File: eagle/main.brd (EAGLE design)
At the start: 100 x 95 mm, 31 parts, among them IC1 STM32F103, IC2 LM1117, Q1 8MHz

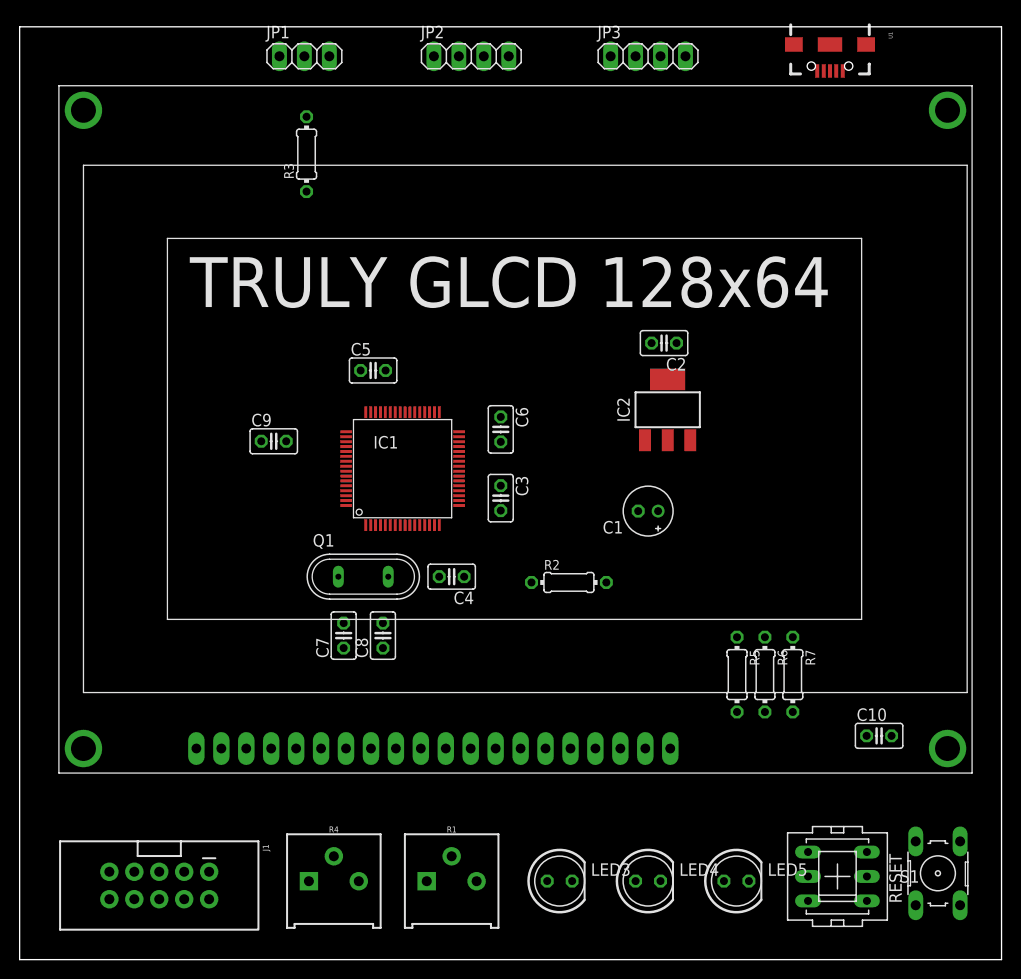
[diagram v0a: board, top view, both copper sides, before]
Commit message: Route some nets in the main board
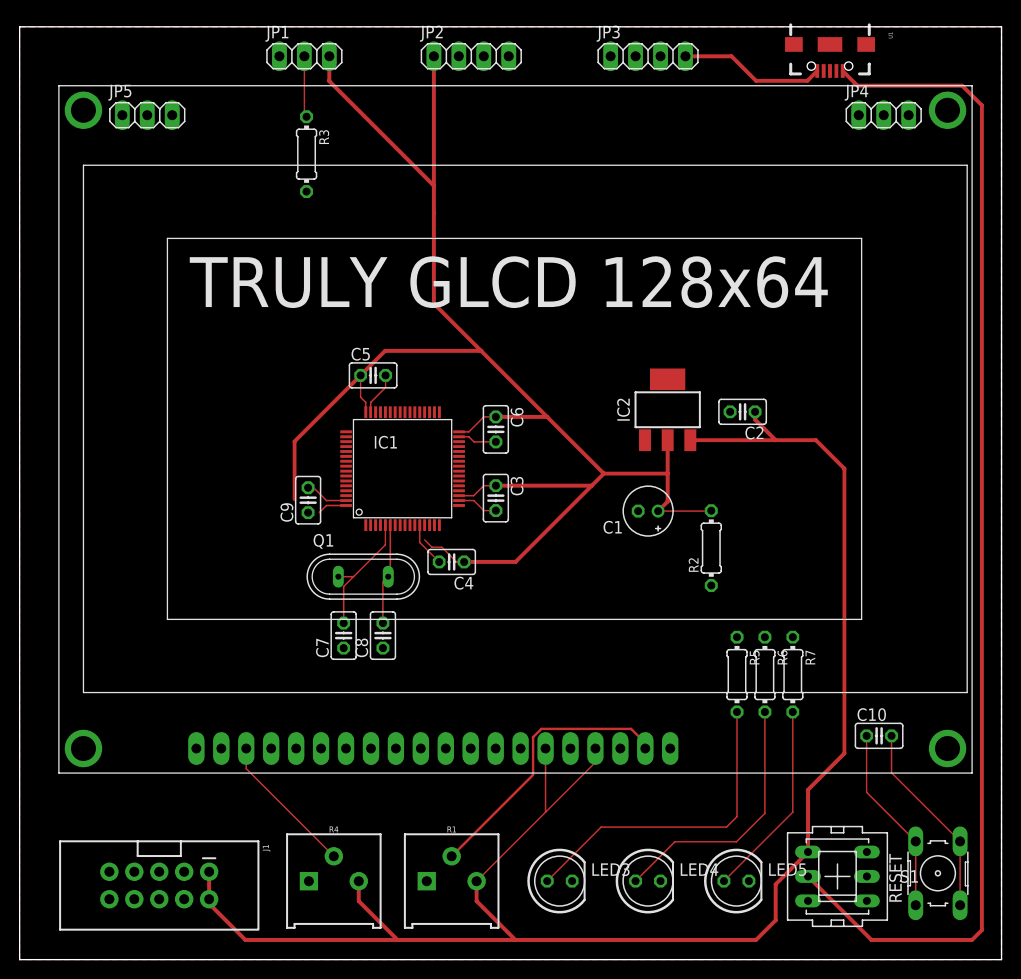
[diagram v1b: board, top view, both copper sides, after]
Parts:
- added JP4, JP5: (no value), pinhead:1X03
- moved R2 14.9 mm to (70.4, 41.9), turned to 90 degrees
- moved C2 10.6 mm to (73.6, 55.8)
- moved C9 6.95 mm to (29.4, 46.8), turned to 90 degrees
- moved C4 1.50 mm to (44.0, 40.5)
- moved C3 0.50 mm to (48.5, 47.0)
- moved C5 0.50 mm to (36.0, 59.5)
- moved C6 0.50 mm to (48.5, 54.0)
- turned R3 to 270 degrees
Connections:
- net N$8 renamed USB_POWER
- net 3.3V: now also JP1.3
- net N$6: no longer JP1.3
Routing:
- net VCC: track 0.00 -> 173.1 mm
- net 3.3V: track 0.00 -> 169.0 mm
- net USB_POWER: track 0.00 -> 120.4 mm
- net GND: track 0.00 -> 56.5 mm
- net N$3: track 0.00 -> 32.7 mm
- net N$1: track 0.00 -> 28.5 mm
- net N$4: track 0.00 -> 26.3 mm
- net N$15: track 0.00 -> 20.1 mm
- net N$6: track 0.00 -> 19.3 mm
- net N$2: track 0.00 -> 14.7 mm
- net N$5: track 0.00 -> 13.3 mm
- net N$7: track 0.00 -> 10.3 mm
- net N$11: track 0.00 -> 6.25 mm
- added copper zone on layer 1, net GND

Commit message: Finish basic routing
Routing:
- net SBDI_DAT: track 0.00 -> 89.8 mm, vias 0 -> 2
- net SBDI_CLK: track 0.00 -> 84.2 mm, vias 0 -> 2
- net SBDI_EN: track 0.00 -> 78.7 mm, vias 0 -> 2
- net TXD: track 0.00 -> 67.7 mm, vias 0 -> 3
- net RXD: track 0.00 -> 67.3 mm, vias 0 -> 3
- net N$6: track 19.3 -> 84.1 mm
- net N$10: track 0.00 -> 56.4 mm, vias 0 -> 3
- net VCC: track 173.1 -> 228.6 mm
- net N$9: track 0.00 -> 47.9 mm, vias 0 -> 2
- net SWCLK: track 0.00 -> 47.4 mm, vias 0 -> 4
- net SWDIO: track 0.00 -> 43.4 mm, vias 0 -> 1
- net N$13: track 0.00 -> 43.2 mm, vias 0 -> 2
- net DB6: track 0.00 -> 42.5 mm, vias 0 -> 1
- net DB5: track 0.00 -> 42.3 mm, vias 0 -> 1
- net DB7: track 0.00 -> 41.6 mm, vias 0 -> 1
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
